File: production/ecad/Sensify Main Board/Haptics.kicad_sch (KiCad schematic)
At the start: 12 parts, among them U1 DRV2605LDGSR, U2 DRV2605LDGSR, U3 DRV2605LDGSR, U4 DRV2605LDGSR

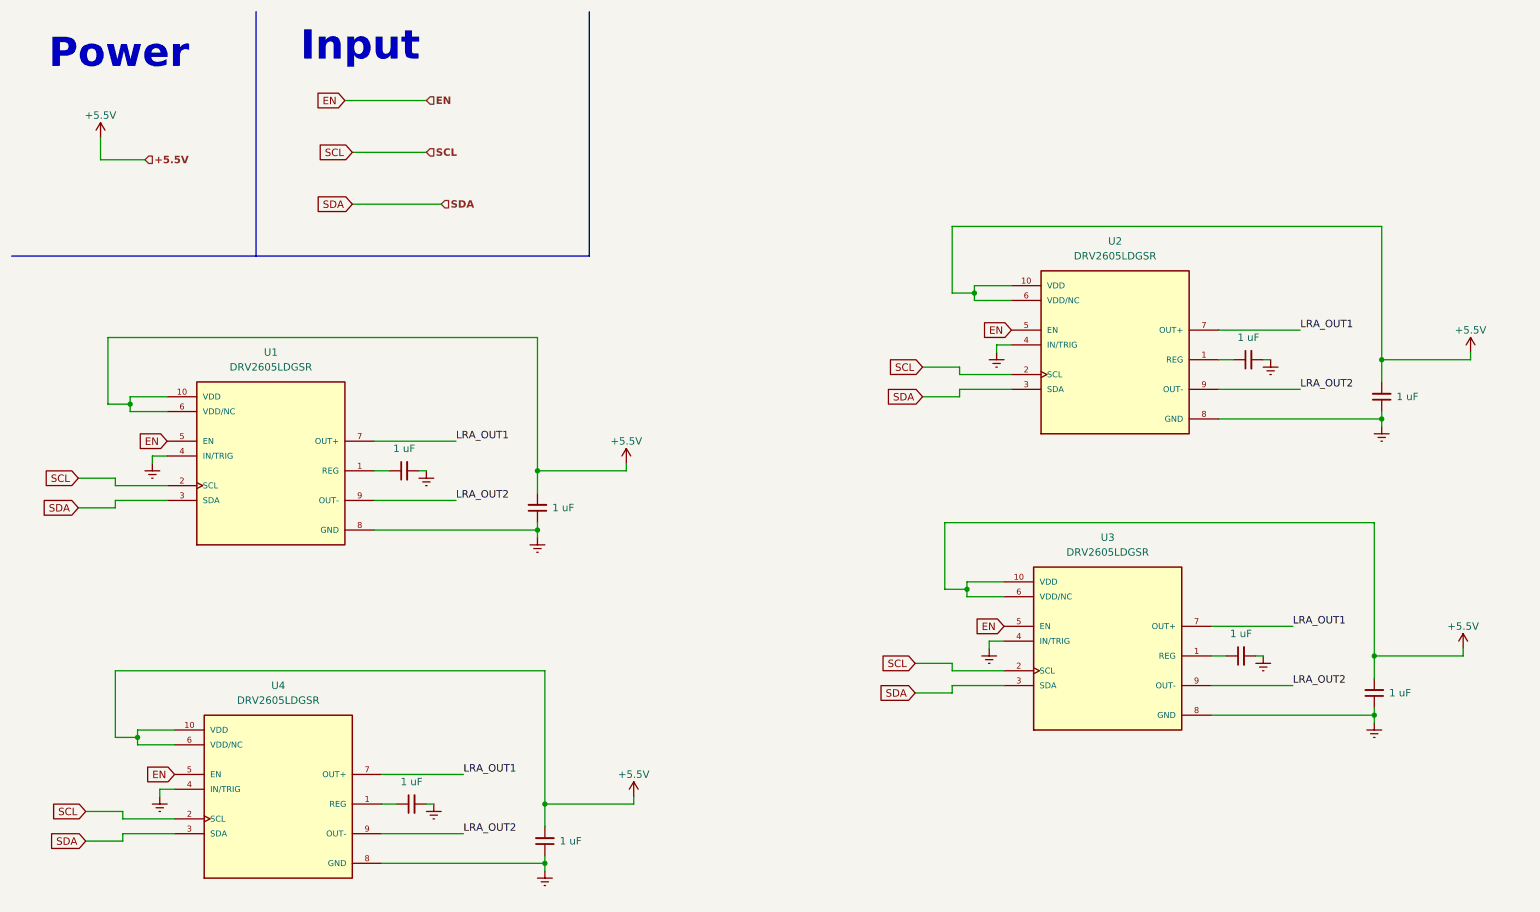
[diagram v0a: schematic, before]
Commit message: added passives footprints & changed 5.5V to 5V
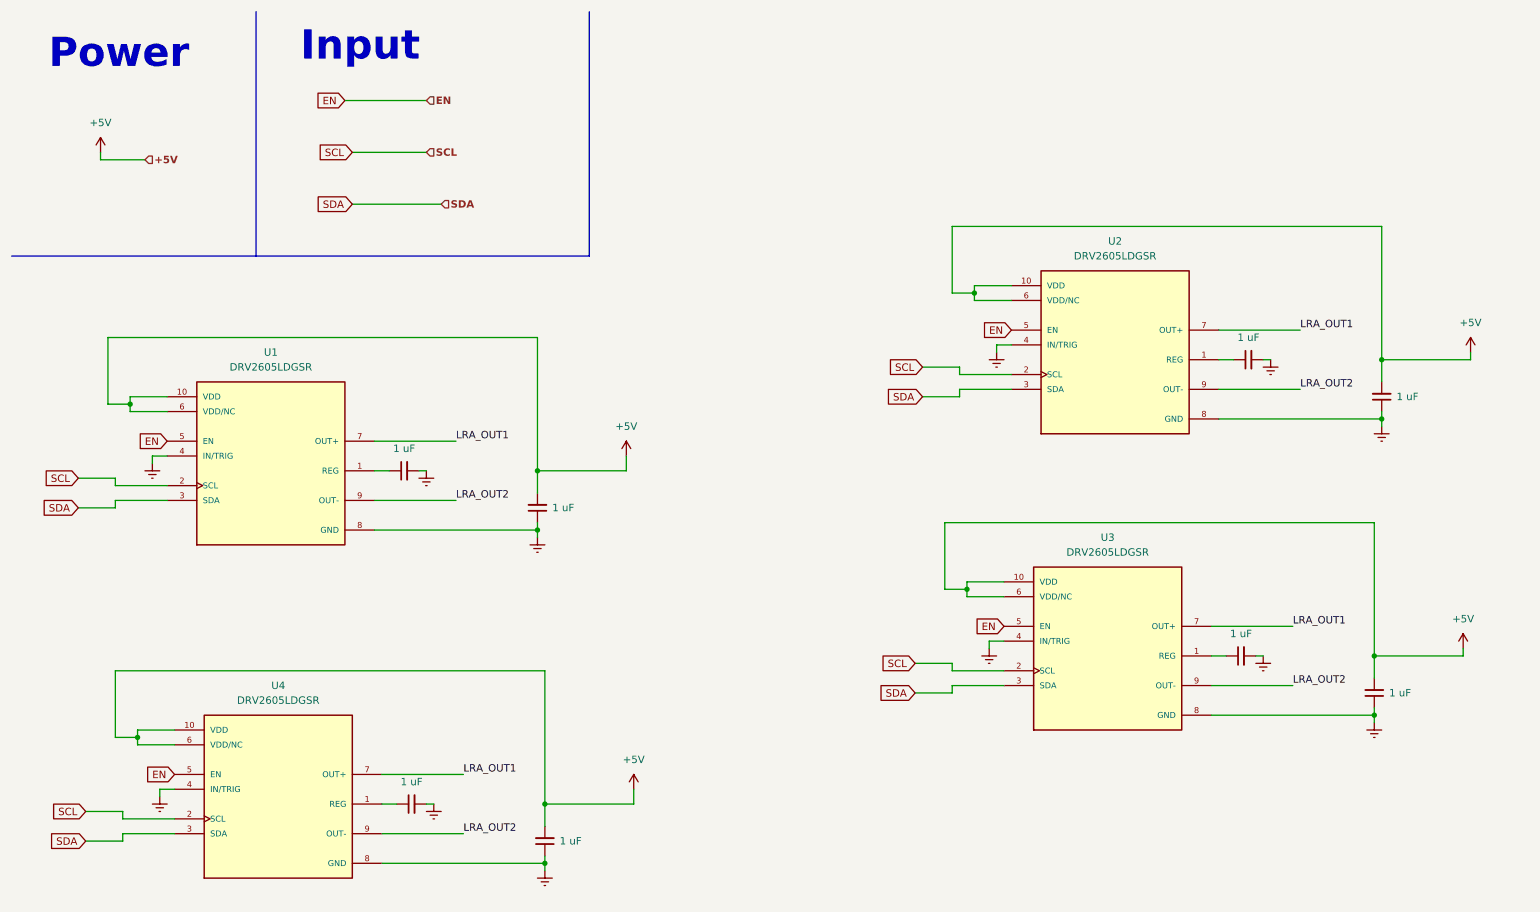
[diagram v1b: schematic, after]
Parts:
- C1, C15, C3, C5: footprint (none) -> Resistor_SMD:R_0402_1005Metric
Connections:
- net VDC renamed +5V

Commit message: added connectors
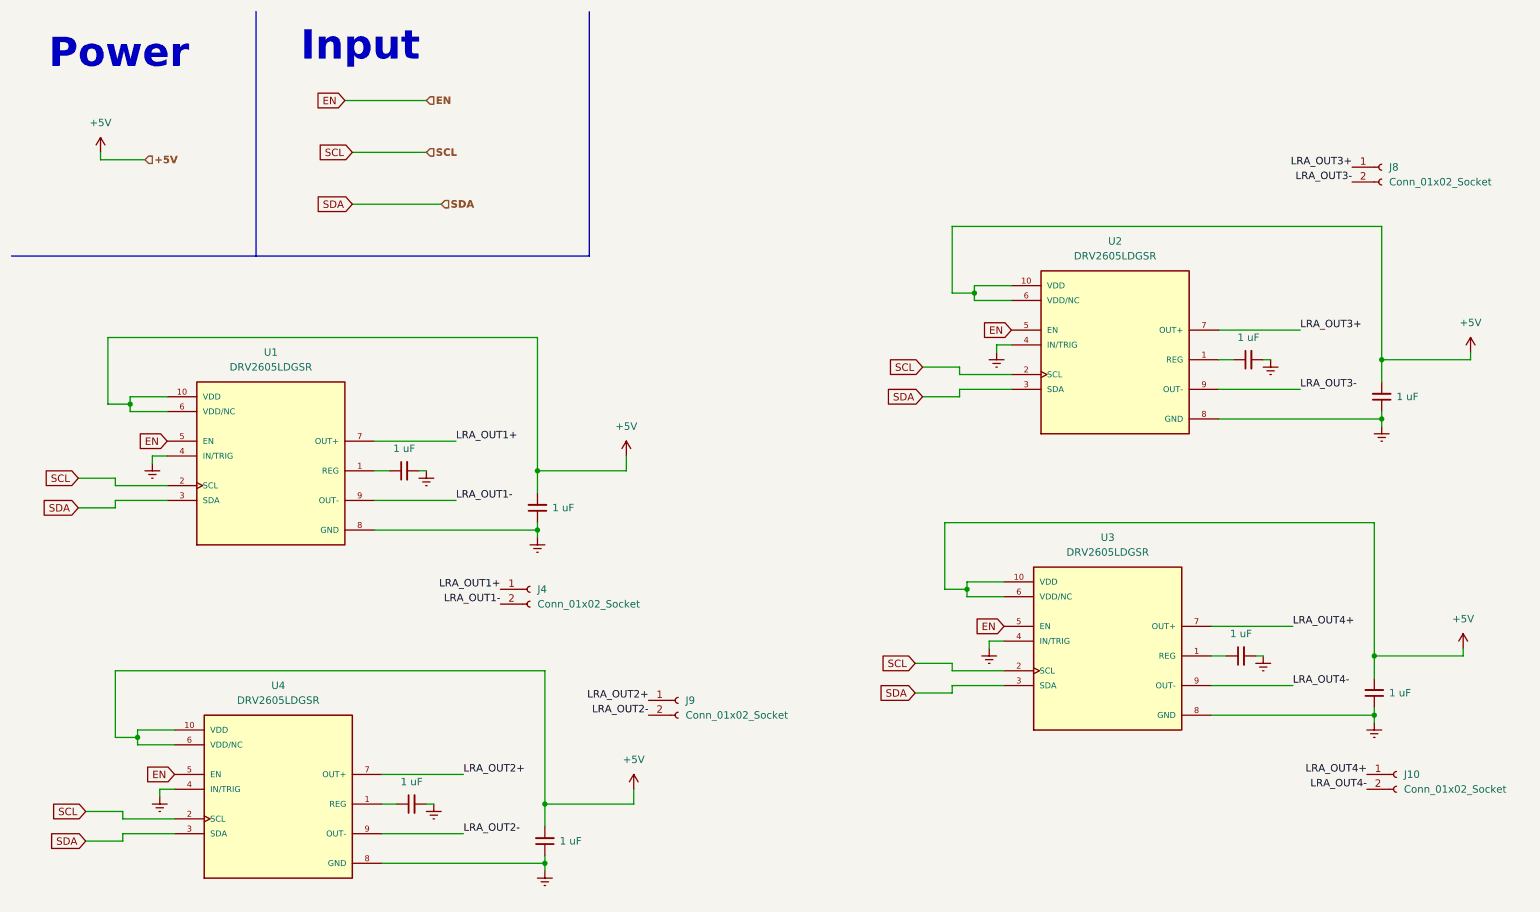
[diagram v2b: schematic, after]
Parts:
- added J10, J4, J8, J9: Conn_01x02_Socket, symbol Connector:Conn_01x02_Socket
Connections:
- removed net LRA_OUT1: U1.7 (OUT+), U2.7 (OUT+), U3.7 (OUT+), U4.7 (OUT+)
- removed net LRA_OUT2: U1.9 (OUT-), U2.9 (OUT-), U3.9 (OUT-), U4.9 (OUT-)
- new net LRA_OUT1+: J4.1 (Pin_1), U1.7 (OUT+)
- new net LRA_OUT1-: J4.2 (Pin_2), U1.9 (OUT-)
- new net LRA_OUT2+: J9.1 (Pin_1), U4.7 (OUT+)
- new net LRA_OUT2-: J9.2 (Pin_2), U4.9 (OUT-)
- new net LRA_OUT3+: J8.1 (Pin_1), U2.7 (OUT+)
- new net LRA_OUT3-: J8.2 (Pin_2), U2.9 (OUT-)
- new net LRA_OUT4+: J10.1 (Pin_1), U3.7 (OUT+)
- new net LRA_OUT4-: J10.2 (Pin_2), U3.9 (OUT-)
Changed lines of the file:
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@@
     (effects (font (size 5 5) (thickness 1) bold) (justify left bottom))
   )
-  (label "LRA_OUT2" (at 232.41 77.47 0) (fields_autoplaced)
+  (label "LRA_OUT1+" (at 95.25 111.76 180) (fields_autoplaced)
+    (effects (font (size 1.27 1.27)) (justify right bottom))
+  )
+  (label "LRA_OUT3-" (at 232.41 77.47 0) (fields_autoplaced)
     (effects (font (size 1.27 1.27)) (justify left bottom))
   )
-  (label "LRA_OUT1" (at 88.9 143.51 0) (fields_autoplaced)
+  (label "LRA_OUT2+" (at 120.65 130.81 180) (fields_autoplaced)
+    (effects (font (size 1.27 1.27)) (justify right bottom))
+  )
+  (label "LRA_OUT2+" (at 88.9 143.51 0) (fields_autoplaced)
     (effects (font (size 1.27 1.27)) (justify left bottom))
   )
-  (label "LRA_OUT1" (at 232.41 67.31 0) (fields_autoplaced)
+  (label "LRA_OUT3-" (at 241.3 41.91 180) (fields_autoplaced)
+    (effects (font (size 1.27 1.27)) (justify right bottom))
+  )
+  (label "LRA_OUT3+" (at 232.41 67.31 0) (fields_autoplaced)
     (effects (font (size 1.27 1.27)) (justify left bottom))
   )
-  (label "LRA_OUT1" (at 231.14 118.11 0) (fields_autoplaced)
+  (label "LRA_OUT1-" (at 95.25 114.3 180) (fields_autoplaced)
+    (effects (font (size 1.27 1.27)) (justify right bottom))
+  )
+  (label "LRA_OUT3+" (at 241.3 39.37 180) (fields_autoplaced)
+    (effects (font (size 1.27 1.27)) (justify right bottom))
+  )
+  (label "LRA_OUT4+" (at 231.14 118.11 0) (fields_autoplaced)
     (effects (font (size 1.27 1.27)) (justify left bottom))
   )
-  (label "LRA_OUT2" (at 88.9 153.67 0) (fields_autoplaced)
+  (label "LRA_OUT2-" (at 120.65 133.35 180) (fields_autoplaced)
+    (effects (font (size 1.27 1.27)) (justify right bottom))
+  )
+  (label "LRA_OUT2-" (at 88.9 153.67 0) (fields_autoplaced)
     (effects (font (size 1.27 1.27)) (justify left bottom))
   )
-  (label "LRA_OUT1" (at 87.63 86.36 0) (fields_autoplaced)
+  (label "LRA_OUT1+" (at 87.63 86.36 0) (fields_autoplaced)
     (effects (font (size 1.27 1.27)) (justify left bottom))
   )
-  (label "LRA_OUT2" (at 87.63 96.52 0) (fields_autoplaced)
+  (label "LRA_OUT4+" (at 243.84 143.51 180) (fields_autoplaced)
+    (effects (font (size 1.27 1.27)) (justify right bottom))
+  )
+  (label "LRA_OUT1-" (at 87.63 96.52 0) (fields_autoplaced)
     (effects (font (size 1.27 1.27)) (justify left bottom))
   )
-  (label "LRA_OUT2" (at 231.14 128.27 0) (fields_autoplaced)
+  (label "LRA_OUT4-" (at 231.14 128.27 0) (fields_autoplaced)
     (effects (font (size 1.27 1.27)) (justify left bottom))
+  )
+  (label "LRA_OUT4-" (at 243.84 146.05 180) (fields_autoplaced)
+    (effects (font (size 1.27 1.27)) (justify right bottom))
   )
   (global_label "SDA" (shape input) (at 24.13 154.94 180) (fields_autoplaced)
@@
     )
   )
+  (symbol (lib_id "Connector:Conn_01x02_Socket") (at 125.73 130.81 0) (unit 1)
+    (in_bom yes) (on_board yes) (dnp no) (fields_autoplaced)
+    (property "Reference" "J9" (at 127 130.81 0)
+      (effects (font (size 1.27 1.27)) (justify left))
+    )
+    (property "Value" "Conn_01x02_Socket" (at 127 133.35 0)
+      (effects (font (size 1.27 1.27)) (justify left))
+    )
+    (property "Footprint" "" (at 125.73 130.81 0)
+      (effects (font (size 1.27 1.27)) hide)
+    )
+    (property "Datasheet" "~" (at 125.73 130.81 0)
+      (effects (font (size 1.27 1.27)) hide)
+    )
+    (pin "1")
+    (pin "2")
+    (instances
+      (project "Sensify Main Board"
+        (path "/9a7ba7c3-7d28-4a83-bdbc-38fbff59fcbe/326628ab-ecd6-4a75-a8ad-db965643b25a"
+          (reference "J9") (unit 1)
+        )
+      )
+    )
+  )
   (symbol (lib_id "power:+5V") (at 26.67 36.83 0) (unit 1)
     (in_bom yes) (on_board yes) (dnp no) (fields_autoplaced)
@@
         (path "/9a7ba7c3-7d28-4a83-bdbc-38fbff59fcbe/326628ab-ecd6-4a75-a8ad-db965643b25a"
           (reference "#PWR010") (unit 1)
+        )
+      )
+    )
+  )
+  (symbol (lib_id "Connector:Conn_01x02_Socket") (at 100.33 111.76 0) (unit 1)
+    (in_bom yes) (on_board yes) (dnp no) (fields_autoplaced)
+    (property "Reference" "J4" (at 101.6 111.76 0)
+      (effects (font (size 1.27 1.27)) (justify left))
+    )
+    (property "Value" "Conn_01x02_Socket" (at 101.6 114.3 0)
+      (effects (font (size 1.27 1.27)) (justify left))
+    )
+    (property "Footprint" "" (at 100.33 111.76 0)
+      (effects (font (size 1.27 1.27)) hide)
+    )
+    (property "Datasheet" "~" (at 100.33 111.76 0)
+      (effects (font (size 1.27 1.27)) hide)
+    )
+    (pin "1")
+    (pin "2")
+    (instances
+      (project "Sensify Main Board"
+        (path "/9a7ba7c3-7d28-4a83-bdbc-38fbff59fcbe/326628ab-ecd6-4a75-a8ad-db965643b25a"
+          (reference "J4") (unit 1)
         )
       )
@@
     )
   )
+  (symbol (lib_id "Connector:Conn_01x02_Socket") (at 246.38 39.37 0) (unit 1)
+    (in_bom yes) (on_board yes) (dnp no) (fields_autoplaced)
+    (property "Reference" "J8" (at 247.65 39.37 0)
+      (effects (font (size 1.27 1.27)) (justify left))
+    )
+    (property "Value" "Conn_01x02_Socket" (at 247.65 41.91 0)
+      (effects (font (size 1.27 1.27)) (justify left))
+    )
+    (property "Footprint" "" (at 246.38 39.37 0)
+      (effects (font (size 1.27 1.27)) hide)
+    )
+    (property "Datasheet" "~" (at 246.38 39.37 0)
+      (effects (font (size 1.27 1.27)) hide)
+    )
+    (pin "1")
+    (pin "2")
+    (instances
+      (project "Sensify Main Board"
+        (path "/9a7ba7c3-7d28-4a83-bdbc-38fbff59fcbe/326628ab-ecd6-4a75-a8ad-db965643b25a"
+          (reference "J8") (unit 1)
+        )
+      )
+    )
+  )
   (symbol (lib_id "Device:C_Small") (at 80.01 148.59 90) (unit 1)
     (in_bom yes) (on_board yes) (dnp no) (fields_autoplaced)
@@
         )
       )
+    )
+  )
+  (symbol (lib_id "Connector:Conn_01x02_Socket") (at 248.92 143.51 0) (unit 1)
+    (in_bom yes) (on_board yes) (dnp no) (fields_autoplaced)
+    (property "Reference" "J10" (at 250.19 143.51 0)
+      (effects (font (size 1.27 1.27)) (justify left))
+    )
+    (property "Value" "Conn_01x02_Socket" (at 250.19 146.05 0)
+      (effects (font (size 1.27 1.27)) (justify left))
+    )
+    (property "Footprint" "" (at 248.92 143.51 0)
+      (effects (font (size 1.27 1.27)) hide)
+    )
+    (property "Datasheet" "~" (at 248.92 143.51 0)
+      (effects (font (size 1.27 1.27)) hide)
+    )
+    (pin "1")
+    (pin "2")
+    (instances
+      (project "Sensify Main Board"
+        (path "/9a7ba7c3-7d28-4a83-bdbc-38fbff59fcbe/326628ab-ecd6-4a75-a8ad-db965643b25a"
+          (reference "J10") (unit 1)
+        )
+      )

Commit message: Finished IMU, Haptics, MCU, and Root Page
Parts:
- added TP9: TestPoint, symbol Connector:TestPoint
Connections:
- net EN renamed HAPTICS_EN
- net HAPTICS_EN: now also TP9.1
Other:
- note added: "CONNECTORS"
- note added: "HAPTIC DRIVERS"
- note added: "TEST POINTS"
- moved on the sheet: J10, J4, J8, J9, U1, U2, U3, U4

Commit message: changed footprint path
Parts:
- U1, U2, U3, U4: footprint footprints:SOP50P490X110-10N -> Sensify Footprints:SOP50P490X110-10N
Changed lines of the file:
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@@
       (effects (font (size 1.27 1.27)))
     )
-    (property "Footprint" "footprints:SOP50P490X110-10N" (at 53.34 91.44 0)
+    (property "Footprint" "Sensify Footprints:SOP50P490X110-10N" (at 53.34 91.44 0)
       (effects (font (size 1.27 1.27)) (justify bottom) hide)
     )
@@
       (effects (font (size 1.27 1.27)))
     )
-    (property "Footprint" "footprints:SOP50P490X110-10N" (at 184.15 92.71 0)
+    (property "Footprint" "Sensify Footprints:SOP50P490X110-10N" (at 184.15 92.71 0)
       (effects (font (size 1.27 1.27)) (justify bottom) hide)
     )
@@
       (effects (font (size 1.27 1.27)))
     )
-    (property "Footprint" "footprints:SOP50P490X110-10N" (at 54.61 148.59 0)
+    (property "Footprint" "Sensify Footprints:SOP50P490X110-10N" (at 54.61 148.59 0)
       (effects (font (size 1.27 1.27)) (justify bottom) hide)
     )
@@
       (effects (font (size 1.27 1.27)))
     )
-    (property "Footprint" "footprints:SOP50P490X110-10N" (at 182.88 143.51 0)
-      (effects (font (size 1.27 1.27)) (justify bottom) hide)
-    )
+    (property "Footprint" "Sensify Footprints:SOP50P490X110-10N" (at 182.88 143.51 0)
+      (effects (font (size 1.27 1.27)) (justify bottom) hide)
+    )

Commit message: connectors footprint
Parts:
- J10, J4, J8, J9: footprint (none) -> Connector_JST:JST_EH_B2B-EH-A_1x02_P2.50mm_Vertical
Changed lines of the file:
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@@
       (effects (font (size 1.27 1.27)) (justify left))
     )
-    (property "Footprint" "" (at 130.81 40.64 0)
+    (property "Footprint" "Connector_JST:JST_EH_B2B-EH-A_1x02_P2.50mm_Vertical" (at 130.81 40.64 0)
       (effects (font (size 1.27 1.27)) hide)
     )
@@
       (effects (font (size 1.27 1.27)) (justify left))
     )
-    (property "Footprint" "" (at 130.81 31.75 0)
+    (property "Footprint" "Connector_JST:JST_EH_B2B-EH-A_1x02_P2.50mm_Vertical" (at 130.81 31.75 0)
       (effects (font (size 1.27 1.27)) hide)
     )
@@
       (effects (font (size 1.27 1.27)) (justify left))
     )
-    (property "Footprint" "" (at 170.18 31.75 0)
+    (property "Footprint" "Connector_JST:JST_EH_B2B-EH-A_1x02_P2.50mm_Vertical" (at 170.18 31.75 0)
       (effects (font (size 1.27 1.27)) hide)
     )
@@
       (effects (font (size 1.27 1.27)) (justify left))
     )
-    (property "Footprint" "" (at 170.18 40.64 0)
-      (effects (font (size 1.27 1.27)) hide)
-    )
+    (property "Footprint" "Connector_JST:JST_EH_B2B-EH-A_1x02_P2.50mm_Vertical" (at 170.18 40.64 0)
+      (effects (font (size 1.27 1.27)) hide)
+    )
